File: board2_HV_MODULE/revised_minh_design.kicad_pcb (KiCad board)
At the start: 2 copper layers, 100 x 42.2 mm, 13 parts, among them J1 Conn_01x07_Male, U1 LM7805_TO220, U2 NE5532, U3 CB101

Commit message: -
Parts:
- added R5: 2K, Resistor_THT:R_Axial_DIN0309_L9.0mm_D3.2mm_P15.24mm_Horizontal, B.Cu at (120.8, 55.3)
- added R6: 1.1K, Resistor_THT:R_Axial_DIN0309_L9.0mm_D3.2mm_P15.24mm_Horizontal, B.Cu at (138.3, 55.3)
- added R7: 2K, Resistor_THT:R_Axial_DIN0309_L9.0mm_D3.2mm_P15.24mm_Horizontal, B.Cu at (120.7, 59.1)
- added R8: 1.1K, Resistor_THT:R_Axial_DIN0309_L9.0mm_D3.2mm_P15.24mm_Horizontal, B.Cu at (138.2, 59.0)
- moved R4 45.3 mm to (155.6, 59.1), turned to 180 degrees
- moved D2 11.5 mm to (111.1, 60.9), turned to 180 degrees
- moved R1 4.01 mm to (87.4, 61.0)
- moved R2 4.01 mm to (87.4, 57.2)
- moved D1 1.12 mm to (126.7, 57.0)
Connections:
- J1 pad 4: VMON -> VMON_3V3
- J1 pad 5: IMON -> IMON_3V3

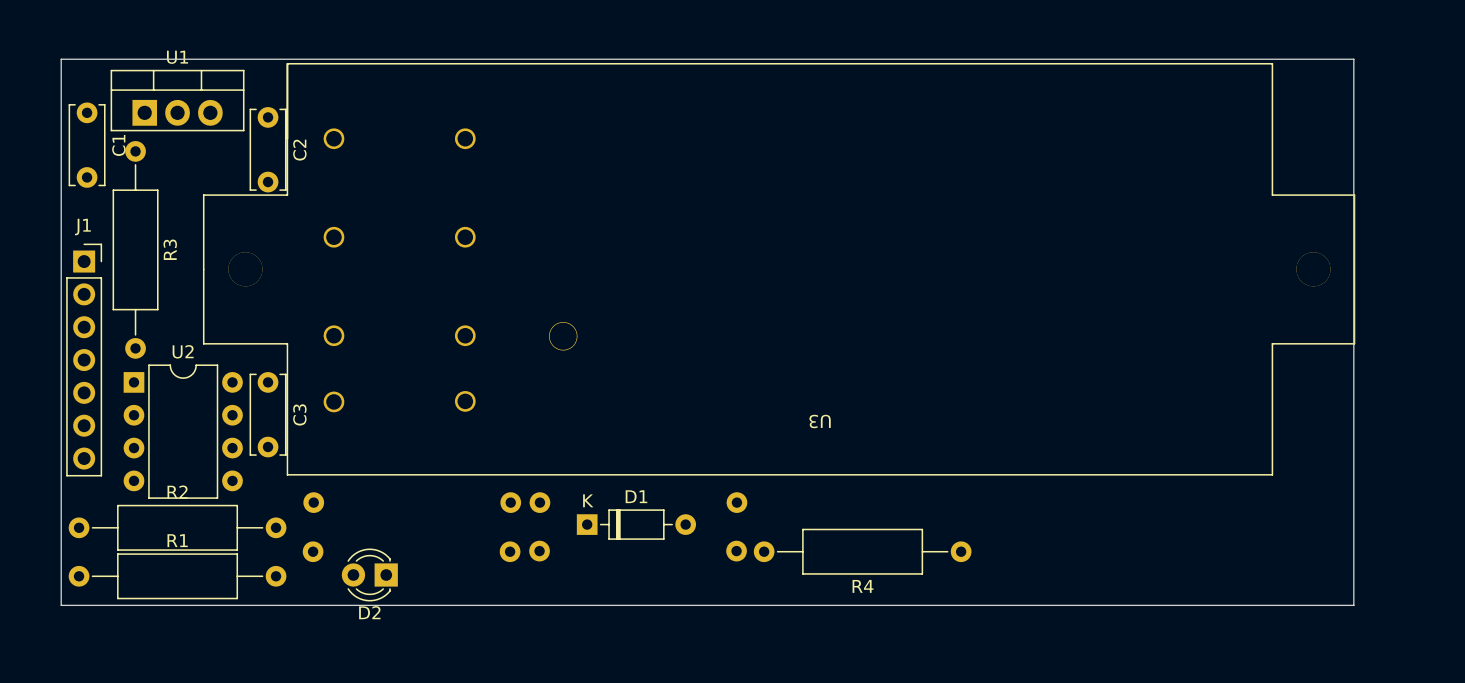
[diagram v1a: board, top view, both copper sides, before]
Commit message: HV Module routed, some footprint changes
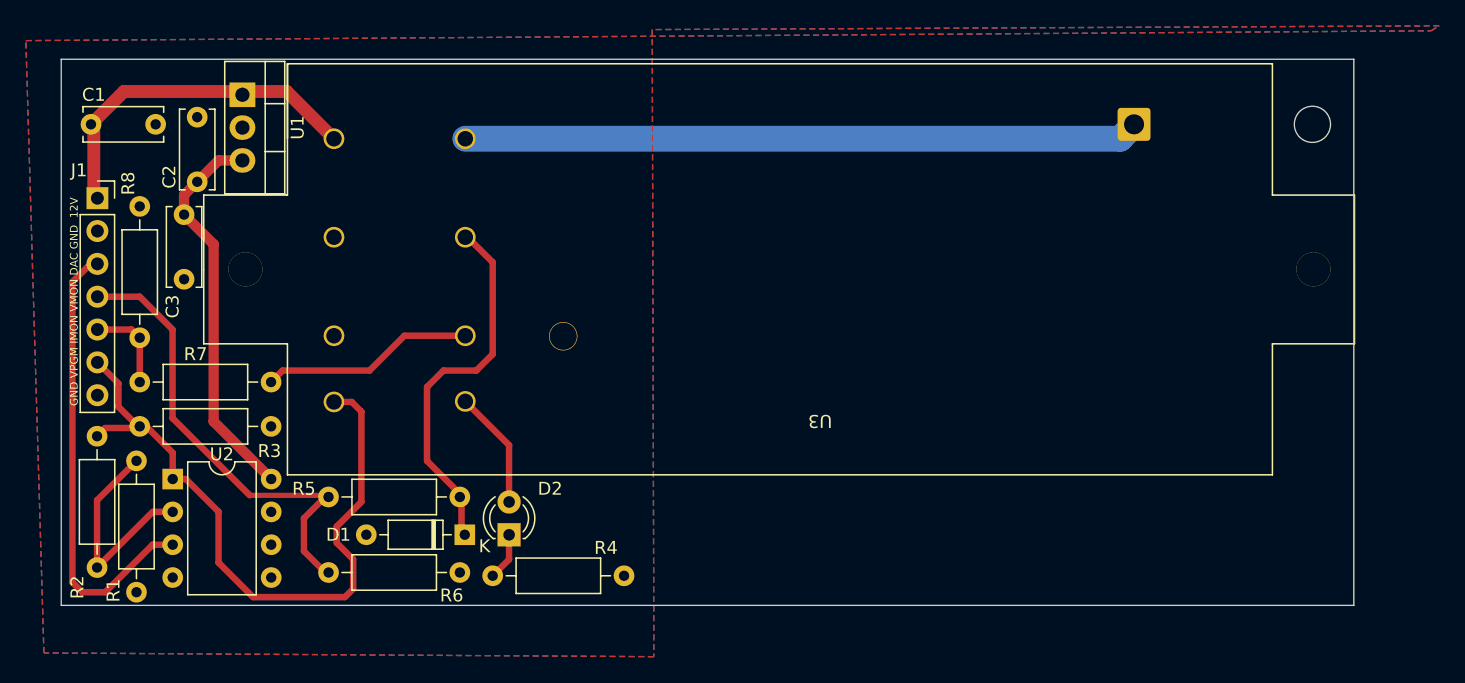
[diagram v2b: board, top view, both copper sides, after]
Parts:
- added J2: Conn_01x01_Male, Connector_Wire:SolderWire-0.75sqmm_1x01_D1.25mm_OD2.3mm_Relief, B.Cu at (169.0, 26.0)
- R1, R2, R3, R4: footprint Resistor_THT:R_Axial_DIN0309_L9.0mm_D3.2mm_P15.24mm_Horizontal -> Resistor_THT:R_Axial_DIN0207_L6.3mm_D2.5mm_P10.16mm_Horizontal
- R5, R6, R7, R8: footprint Resistor_THT:R_Axial_DIN0309_L9.0mm_D3.2mm_P15.24mm_Horizontal -> Resistor_THT:R_Axial_DIN0207_L6.3mm_D2.5mm_P10.16mm_Horizontal; moved to F.Cu
- moved R8 53.3 mm to (92.1, 32.4), turned to -90 degrees
- moved R7 31.5 mm to (92.1, 46.0), turned to 0 degrees
- moved R4 26.1 mm to (129.5, 61.0)
- moved R3 23.7 mm to (102.2, 49.4), turned to 180 degrees
- moved R6 22.1 mm to (116.8, 60.7)
- moved C3 14.5 mm to (95.5, 33.0)
- moved R5 14.1 mm to (106.7, 54.9), turned to 0 degrees
- moved D2 10.00 mm to (120.7, 57.8), turned to 90 degrees
- moved R1 9.97 mm to (91.8, 52.1), turned to -90 degrees
- moved D1 9.50 mm to (117.2, 57.8), turned to 180 degrees
- moved U2 8.05 mm to (94.6, 53.5)
- moved U1 7.69 mm to (100.0, 23.7), turned to -90 degrees
- moved C2 7.40 mm to (96.5, 30.5), turned to 90 degrees
- moved J1 5.01 mm to (88.8, 31.8)
- moved R2 3.38 mm to (88.8, 60.3), turned to 90 degrees
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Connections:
- J1 pad 7: VDIV -> Earth
- U3 pad 8: unconnected-(U3-Pad8) -> Net-(U3-Pad8)
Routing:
- net VPGM: track 0.00 -> 53.2 mm
- net Net-(U3-Pad8): track 0.00 -> 52.3 mm
- net VMON_3V3: track 0.00 -> 36.8 mm
- net DAC_SIG: track 0.00 -> 34.8 mm
- net +5V: track 0.00 -> 30.4 mm
- net VMON: track 0.00 -> 28.9 mm
- net +12V: track 0.00 -> 27.3 mm
- net Net-(R1-Pad1): track 0.00 -> 17.2 mm
- net IMON: track 0.00 -> 16.5 mm
- net Net-(D2-Pad2): track 0.00 -> 9.18 mm
- net IMON_3V3: track 0.00 -> 7.88 mm
- net Net-(D2-Pad1): track 0.00 -> 3.70 mm
- added copper zone on B.Cu, net Earth
- added copper zone on F.Cu, net Earth
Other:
- board text added: "GND VPGM IMON VMON DAC GND 12V"

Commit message: JLCPB Submission. Name added, connectors changed to double layer
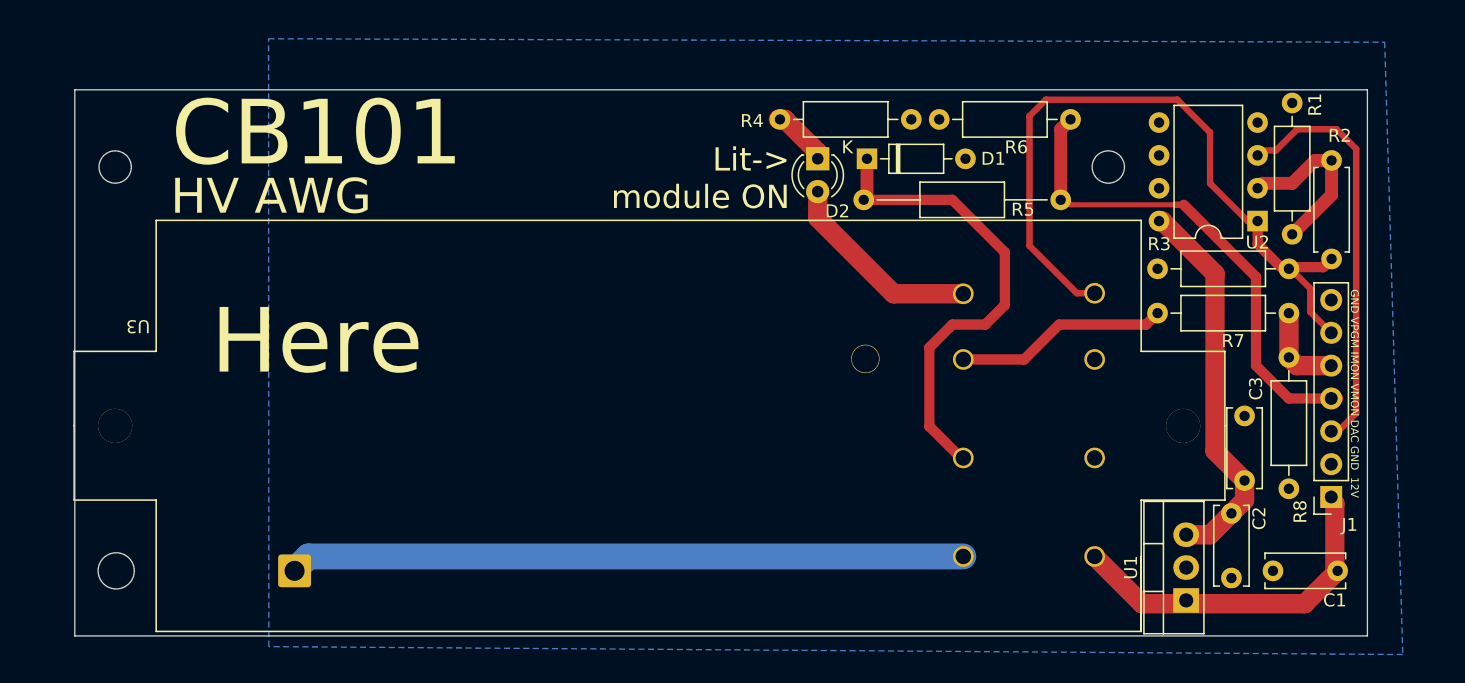
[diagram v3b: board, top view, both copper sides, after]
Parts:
- added  : MountingHole_2.5mm, MountingHole:MountingHole_2.5mm, F.Cu at (167.0, 29.3)
- added  : MountingHole_2.5mm, MountingHole:MountingHole_2.5mm, F.Cu at (90.2, 29.3)
- R2: footprint Resistor_THT:R_Axial_DIN0207_L6.3mm_D2.5mm_P10.16mm_Horizontal -> Resistor_THT:R_Axial_DIN0207_L6.3mm_D2.5mm_P7.62mm_Horizontal
- R5: footprint Resistor_THT:R_Axial_DIN0207_L6.3mm_D2.5mm_P10.16mm_Horizontal -> Resistor_THT:R_Axial_DIN0207_L6.3mm_D2.5mm_P15.24mm_Horizontal
- moved C1 102.4 mm to (184.7, 60.6), turned to 180 degrees
- moved R2 100.6 mm to (184.3, 28.8), turned to -90 degrees
- moved J1 98.2 mm to (184.3, 54.9), turned to 180 degrees
- moved R8 91.5 mm to (181.0, 54.2), turned to 90 degrees
- moved R1 91.1 mm to (181.2, 34.5), turned to 90 degrees
- moved R7 89.1 mm to (181.0, 40.6), turned to 180 degrees
- moved U2 86.3 mm to (178.6, 33.5), turned to 180 degrees
- moved C3 84.6 mm to (177.5, 53.6), turned to 90 degrees
- moved C2 84.0 mm to (176.5, 56.1), turned to -90 degrees
- moved U1 82.8 mm to (173.0, 62.9), turned to 90 degrees
- moved U3 81.5 mm to (176.1, 33.5), turned to 180 degrees
- moved J2 73.6 mm to (104.1, 60.6), turned to 90 degrees
- moved R3 69.7 mm to (170.8, 37.2), turned to 0 degrees
- moved R5 61.1 mm to (163.3, 31.9), turned to 180 degrees
- moved R6 51.0 mm to (153.9, 25.7), turned to 0 degrees
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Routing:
- net VMON: track 28.9 -> 36.8 mm
- net Net-(D2-Pad2): track 9.18 -> 15.7 mm
- net Net-(R1-Pad1): track 17.2 -> 13.6 mm
- net DAC_SIG: track 34.8 -> 31.5 mm
- net VPGM: track 53.2 -> 55.9 mm
- net VMON_3V3: track 36.8 -> 38.1 mm
- net Net-(D2-Pad1): track 3.70 -> 4.74 mm
- net IMON_3V3: track 7.88 -> 6.97 mm
- removed copper zone on F.Cu, net Earth
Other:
- board text added: "CB101 Here"
- board text added: "HV AWG"
- board text added: "Lit-> module ON"

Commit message: JLCPB Submission. Name added, connectors changed to double layer, rounded corners
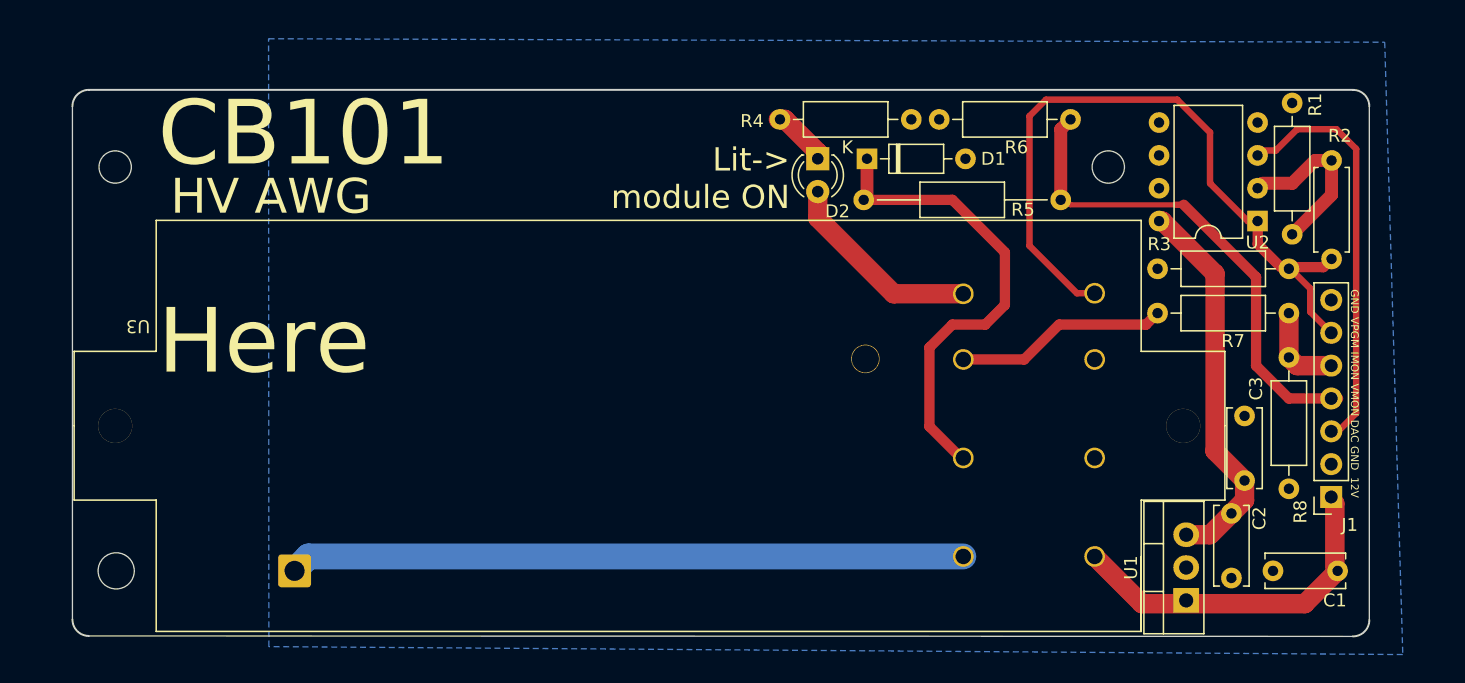
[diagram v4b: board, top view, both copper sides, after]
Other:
- board size 100 x 42.2 mm -> 100.3 x 42.3 mm
- board text added: "S.H.V.R.I.M.P.S"
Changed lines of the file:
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@@
       (drillshape 0)
       (scaleselection 1)
-      (outputdirectory "./")
+      (outputdirectory "Gerber/")
     )
   )
@@
     )
   )
-  (gr_rect (start 87.05 65.614) (end 187.05 23.364) (layer "Edge.Cuts") (width 0.1) (fill none))
+  (gr_line (start 86.868 24.638) (end 86.868 64.344) (layer "Edge.Cuts") (width 0.1))
+  (gr_arc (start 88.138 65.614) (mid 87.239974 65.242026) (end 86.868 64.344) (layer "Edge.Cuts") (width 0.15))
+  (gr_line (start 185.928 23.368) (end 88.138 23.368) (layer "Edge.Cuts") (width 0.15))
+  (gr_arc (start 187.198 64.379974) (mid 186.826026 65.278) (end 185.928 65.649974) (layer "Edge.Cuts") (width 0.15))
+  (gr_arc (start 185.928 23.368) (mid 186.826026 23.739974) (end 187.198 24.638) (layer "Edge.Cuts") (width 0.15))
+  (gr_line (start 88.138 65.614) (end 185.928 65.649974) (layer "Edge.Cuts") (width 0.1))
+  (gr_line (start 187.198 64.379974) (end 187.198 24.638) (layer "Edge.Cuts") (width 0.1))
+  (gr_arc (start 86.868 24.638) (mid 87.239974 23.739974) (end 88.138 23.368) (layer "Edge.Cuts") (width 0.15))
+  (gr_text "S.H.V.R.I.M.P.S" (at 120.65 49.276) (layer "B.SilkS")
+    (effects (font (size 5 5) (thickness 0.7)) (justify mirror))
+  )
   (gr_text "HV AWG" (at 102.235 31.623) (layer "F.SilkS")
     (effects (font (size 2.7 2.7) (thickness 0.6)))
@@
     (effects (font (size 1.8 1.8) (thickness 0.4)) (justify right))
   )
-  (gr_text "CB101\n\nHere" (at 105.791 34.798) (layer "F.SilkS")
-    (effects (font (size 5 5) (thickness 0.8)))
+  (gr_text "CB101\n\nHere" (at 93.472 34.798) (layer "F.SilkS")
+    (effects (font (size 5 5) (thickness 0.8)) (justify left))
   )
   (segment (start 184.531 60.365) (end 184.531 55.372) (width 1.5) (layer "F.Cu") (net 1))
